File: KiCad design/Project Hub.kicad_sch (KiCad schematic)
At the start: 51 parts, among them U1 GL850G-HHGXX(SSOP-28), Y1 12MHz

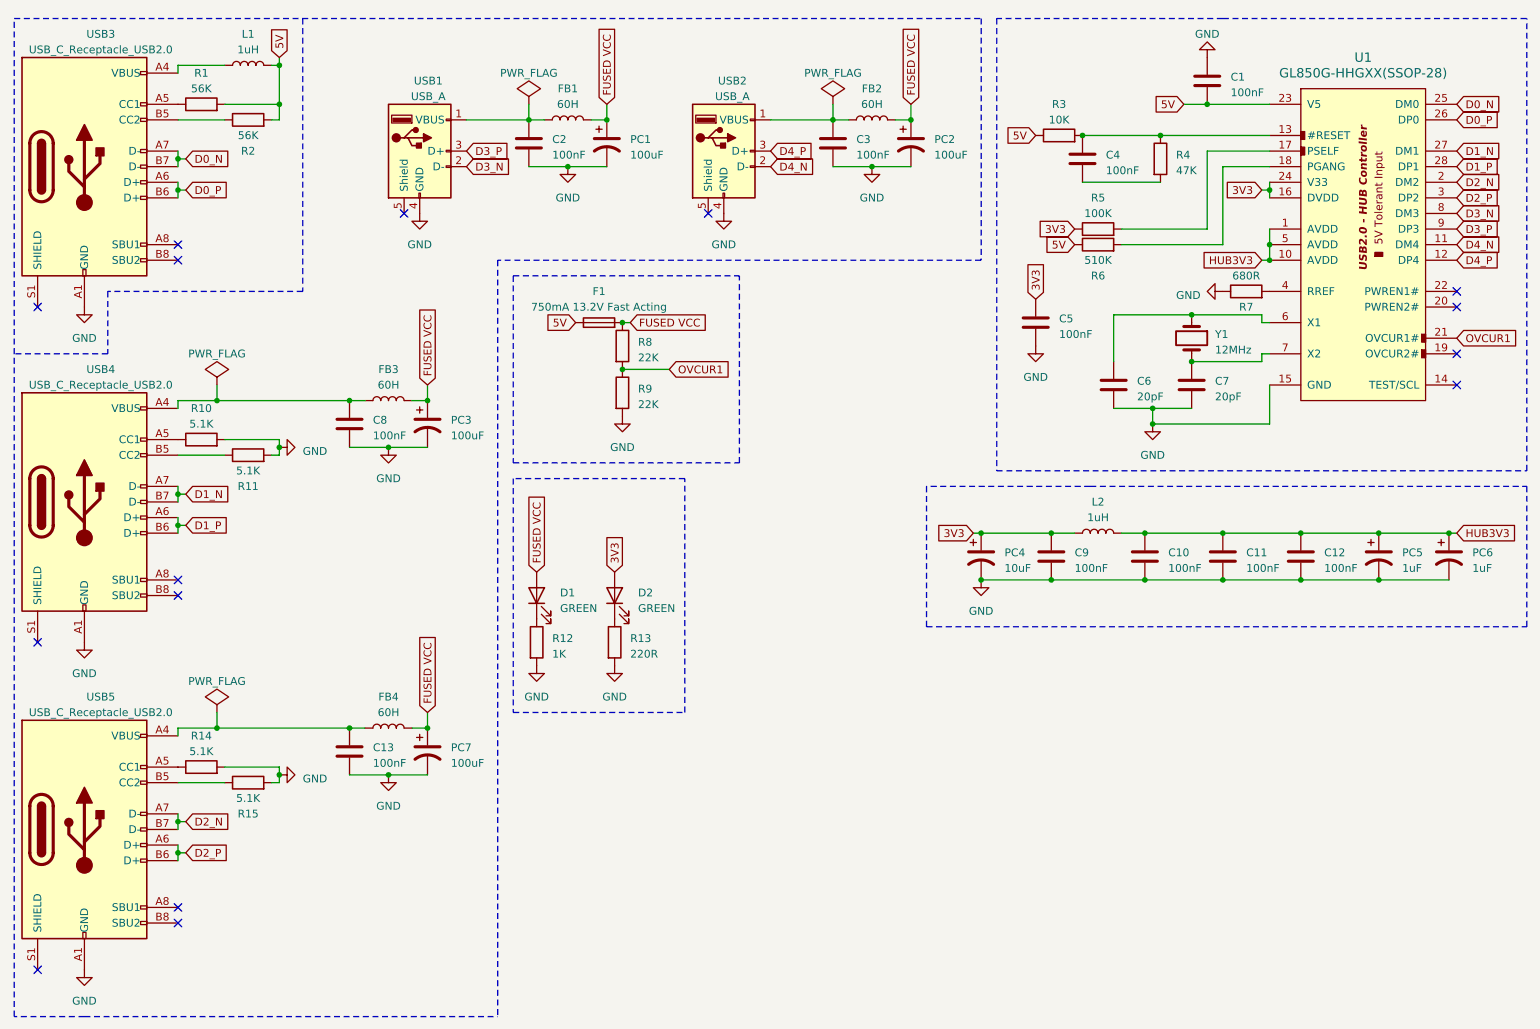
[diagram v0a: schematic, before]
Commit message: fixed upstream port 5.1k resistors
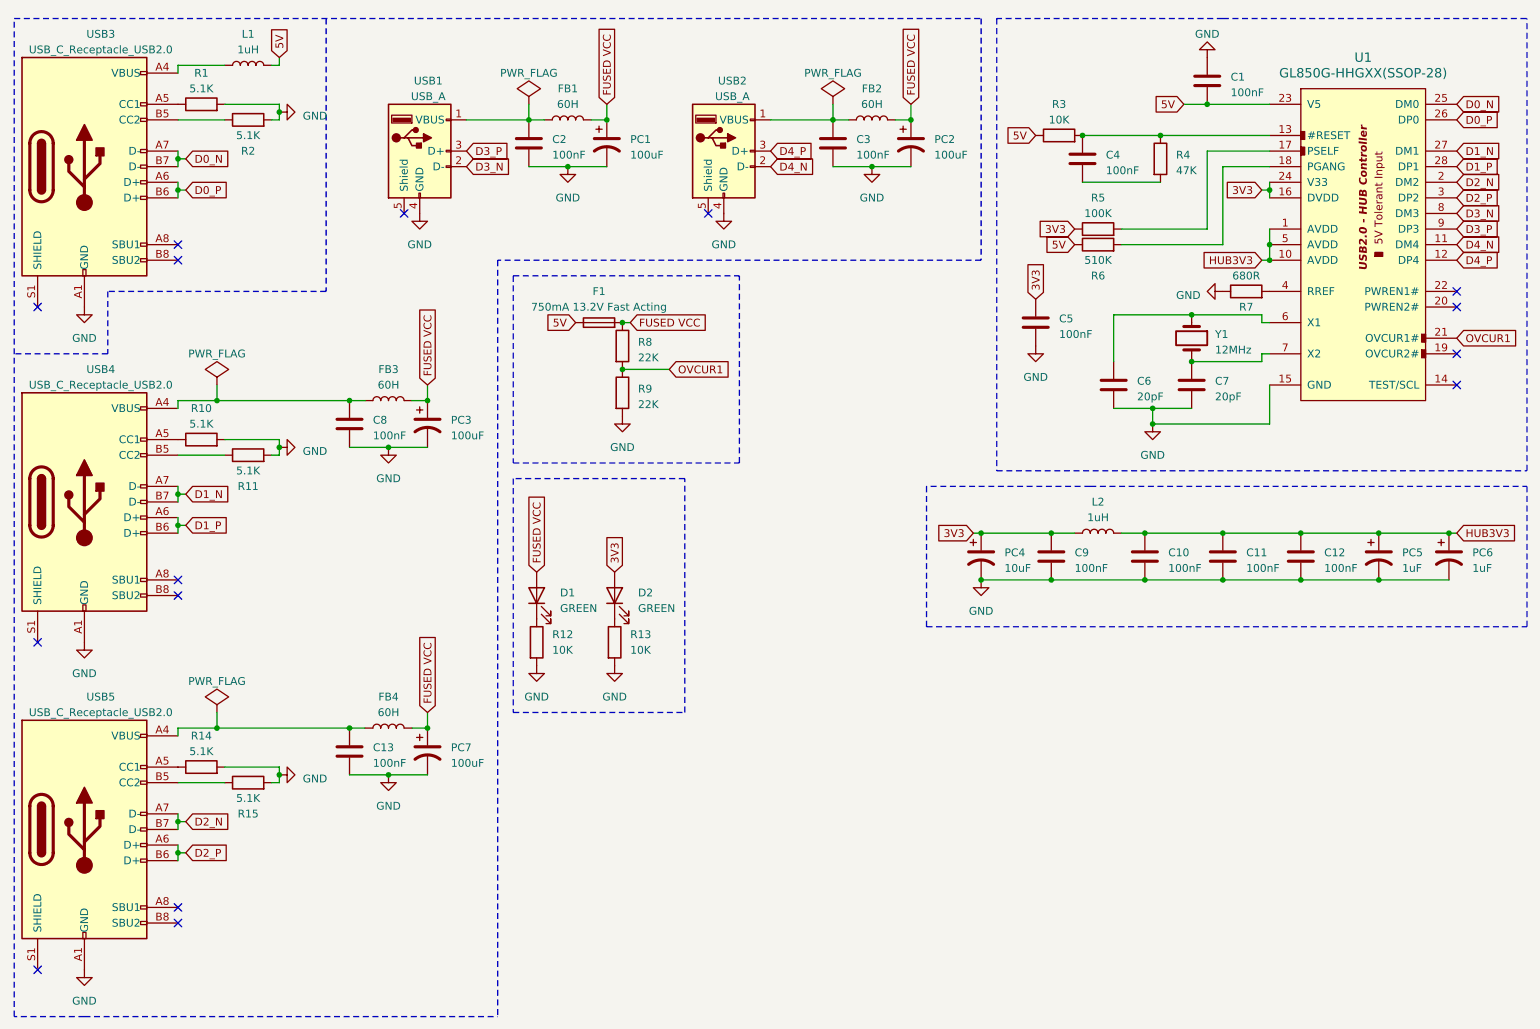
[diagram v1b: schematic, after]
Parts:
- R1, R2: value 56K -> 5.1K
- R12: value 1K -> 10K
- R13: value 220R -> 10K
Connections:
- net 5V: no longer R1.2, R2.2
- net GND: now also R1.2, R2.2
